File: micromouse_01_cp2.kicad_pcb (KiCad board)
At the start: 4 copper layers, 52 x 51.4 mm, 109 parts, among them IC2 MPU-6500, IC5 DRV8835DSSR, IC6 PCA9632TK,118, J1 Conn_01x02_Pin, J2 Fan+, J4 Fan-, M1 MK06-4.5, M2 MK06-4.5, Q1 MCM3400A-TP, Q2 MCM3400A-TP, Q3 MCM3400A-TP, Q4 Q_PMOS_GSD, Q5 Q_PMOS_GSD, Q6 Q_PMOS_GSD, SW3 SSSS810701, U1 SMT-0440-S-R, U10 MA730, U11 MA730, U13 MCP3464T-E/NC, U2 LBR-127HLD, U3 LBR-127HLD, U4 LBR-127HLD, U5 LBR-127HLD, U6 LXDC55FAAA-203, U7 MCP73831-2-OT, U8 WS2812-2020, U9 ESP32-S3-PICO-1-N8R2

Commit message: 新しい部品乗せた
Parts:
- removed the C21 at (151.9, 58.7)
- removed the C22 at (150.3, 58.4)
- removed the C23 at (149.4, 58.4)
- removed the C24 at (148.4, 59.6)
- removed the C6 at (153.8, 62.1)
- removed the C7 at (154.8, 60.3)
- removed the J1 at (147.3, 85.4)
- removed the Q2 at (160.7, 66.1)
- removed the Q3 at (161.3, 100.3)
- removed the R10 at (161.8, 63.8)
- removed the R11 at (161.4, 67.9)
- removed the R12 at (167.7, 69.6)
- removed the R13 at (160.2, 64.3)
- removed the R14 at (158.6, 66.1)
- removed the R15 at (157.6, 66.1)
- removed the R20 at (153.7, 60.0)
- removed the R4 at (143.4, 67.9)
- removed the R5 at (140.4, 63.4)
- removed the R7 at (141.3, 67.7)
- removed the R8 at (144.4, 66.9)
- removed the R9 at (133.3, 68.4)
- removed U13: MCP3464T-E/NC, footprints:UQFN20_NC_MCH
- removed the U2 at (140.9, 59.7)
- removed the U3 at (136.4, 62.3)
- removed the U4 at (165.6, 62.3)
- removed the U5 at (161.1, 59.7)
- added C18: 1u, Capacitor_SMD:C_0402_1005Metric, F.Cu at (148.0, 60.6)
- added C19: 1u, Capacitor_SMD:C_0402_1005Metric, F.Cu at (148.3, 62.5)
- added C2: ~, Capacitor_SMD:C_0402_1005Metric, F.Cu at (140.0, 100.3)
- added C26: 0.1u, Capacitor_SMD:C_0402_1005Metric, F.Cu at (154.5, 59.3)
- added C27: 22u, Capacitor_SMD:C_0603_1608Metric, F.Cu at (143.1, 67.4)
- added C28: 22u, Capacitor_SMD:C_0603_1608Metric, F.Cu at (133.5, 73.0)
- added C29: 22u, Capacitor_SMD:C_0603_1608Metric, F.Cu at (160.7, 68.3)
- added C3: ~, Capacitor_SMD:C_0402_1005Metric, F.Cu at (141.4, 100.8)
- added C30: 22u, Capacitor_SMD:C_0603_1608Metric, F.Cu at (168.7, 72.8)
- added IC3: ADS7066IRTER, footprints:QFN50P300X300X80-17N-D, F.Cu at (151.0, 60.2)
- added J4: Battery, footprints:MK06-4.5, F.Cu at (147.3, 85.6)
- added Q5: SiA519, Package_TO_SOT_SMD:Vishay_PowerPAK_SC70-6L_Dual, F.Cu at (141.0, 65.4)
- added Q6: SiA519, Package_TO_SOT_SMD:Vishay_PowerPAK_SC70-6L_Dual, F.Cu at (133.8, 70.3)
- added Q7: SiA519, Package_TO_SOT_SMD:Vishay_PowerPAK_SC70-6L_Dual, F.Cu at (161.0, 65.4)
- added Q8: SiA519, Package_TO_SOT_SMD:Vishay_PowerPAK_SC70-6L_Dual, F.Cu at (168.4, 69.8)
- added R21: 22, Resistor_SMD:R_0402_1005Metric, F.Cu at (140.7, 67.1)
- added R23: 22, Resistor_SMD:R_0402_1005Metric, F.Cu at (133.5, 71.8)
- added R24: １ｋ, Resistor_SMD:R_0402_1005Metric, F.Cu at (139.9, 63.3)
- added R25: 22, Resistor_SMD:R_0402_1005Metric, F.Cu at (161.8, 67.7)
- added R26: １ｋ, Resistor_SMD:R_0402_1005Metric, F.Cu at (157.3, 66.4)
- added R27: 22, Resistor_SMD:R_0402_1005Metric, F.Cu at (169.2, 71.7)
- added R28: １ｋ, Resistor_SMD:R_0402_1005Metric, F.Cu at (166.6, 67.3)
- added U10: LBR-127HLD, footprints:LBR-127HLD, F.Cu at (161.1, 59.7)
- added U11: LBR-127HLD, footprints:LBR-127HLD, F.Cu at (165.6, 62.3)
- added U8: LBR-127HLD, footprints:LBR-127HLD, F.Cu at (140.9, 59.7)
- added U9: LBR-127HLD, footprints:LBR-127HLD, F.Cu at (136.4, 62.3)
- C17: value 0.1u -> 1u
- D10: renamed from D6; value PWR -> POWER
- Q1: value MCM3400A-TP -> SiA910; footprint footprints:DFN2020-6L_MCE -> Package_TO_SOT_SMD:Vishay_PowerPAK_SC70-6L_Dual
- R1: renamed from R33; value 22 -> 0
- R2: renamed from R32; value 22 -> 0
- R22: value 47k -> １ｋ
- R5: renamed from R17; value 47k -> 47k
- R6: value 1k -> 47k
- moved R22 46.0 mm to (146.6, 59.4), turned to 90 degrees
- moved R6 45.2 mm to (163.8, 101.8)
- moved Q1 39.8 mm to (161.1, 100.2), turned to 0 degrees
- moved C20 28.6 mm to (162.2, 70.0), turned to 90 degrees
- moved U5 26.7 mm to (160.3, 71.2), turned to 180 degrees
- moved R2 2.23 mm to (141.4, 99.9), turned to 180 degrees
- moved C17 1.80 mm to (149.8, 62.8), turned to 180 degrees
- moved R1 1.60 mm to (140.5, 99.0)
- moved C22 1.10 mm to (142.0, 95.3)
- moved R10 0.95 mm to (144.3, 95.0)
- moved IC4 0.85 mm to (159.8, 96.4)
- moved U6 0.60 mm to (142.7, 92.5)
- moved U4 0.34 mm to (168.9, 105.1)
- moved C6 0.23 mm to (140.2, 69.3)
- moved SW1 0.15 mm to (163.1, 103.8)
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- renumbered C14 to C1, C37 to C10, C38 to C11, C41 to C12, C15 to C13, C16 to C14, C9 to C15, C25 to C16, C8 to C20, C19 to C21, C18 to C22, C2 to C23, C13 to C24, C10 to C25, C12 to C4, C3 to C5, C5 to C6, C4 to C7, C20 to C8, C1 to C9, D1 to D2, D4 to D3, D3 to D4, D8 to D5, D9 to D6, D10 to D7, D5 to D8, D7 to D9, IC2 to IC1, IC5 to IC2, IC6 to IC4, J3 to J1, J4 to J3, Q4 to Q2, Q5 to Q3, Q6 to Q4, R28 to R10, R30 to R11, R31 to R12, R24 to R13, R1 to R14, R27 to R15, R2 to R16, R23 to R17, R16 to R18, R18 to R19, R19 to R20, R21 to R3, R3 to R4, R29 to R7, R25 to R8, R26 to R9, SW3 to SW1, U10 to U1, U11 to U2, U9 to U3, U1 to U4, U8 to U5, U7 to U6, U6 to U7
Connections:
- C17 pad 1: VBATT -> +3V3
- D2 pad 2: Net-(D1-A) -> Net-(D2-A)
- J3 pad 1: Net-(J4-Pin_1) -> Net-(J3-Pin_1)
- Q1 pad 2: LED_L -> BUZZER
- Q1 pad 3: Net-(Q1-Pad3) -> Net-(J3-Pin_1)
- Q1 pad 5: LED_FL -> FAN_PWM
- Q1 pad 6: Net-(Q1-Pad6) -> Net-(D2-A)
- R22 pad 1: FAN_PWM -> SENS_L
- R6 pad 1: SENS_L -> GND
- R6 pad 2: GND -> FAN_PWM
- U3 pad 7: IMU_MISO -> IMU_MOSI
- U3 pad 8: IMU_MOSI -> IMU_CLK
- U3 pad 9: IMU_CLK -> IMU_MISO
- U4 pad 2: Net-(D1-A) -> Net-(D2-A)
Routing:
- net GND: track 96.2 -> 49.8 mm, vias 283 -> 230
- net NeoPixel: track 17.0 -> 0.97 mm, vias 0 -> 1
- net Net-(C27-Pad1): track 0.00 -> 12.2 mm, vias 0 -> 2
- net Net-(D2-A): track 0.00 -> 10.5 mm
- net Net-(D1-A): track 10.3 -> 0.00 mm
- net Net-(Q7-Pad6): track 0.00 -> 9.97 mm, vias 0 -> 1
- net VBATT: track 61.3 -> 51.7 mm, vias 3 -> 2
- net Net-(C29-Pad1): track 0.00 -> 9.12 mm, vias 0 -> 1
- net Net-(R5-Pad1): track 8.69 -> 0.00 mm
- net Net-(R13-Pad1): track 8.23 -> 0.00 mm, vias 1 -> 0
- net SENS_FL: track 26.4 -> 18.4 mm
- net Net-(R7-Pad1): track 8.03 -> 0.00 mm
- net Net-(Q5-Pad6): track 0.00 -> 7.62 mm
- net Net-(C28-Pad1): track 0.00 -> 6.61 mm, vias 0 -> 1
- net Net-(Q8-Pad6): track 0.00 -> 6.57 mm
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- added copper zone on F.Cu, net Net-(D7-K)
- removed copper zone on F.Cu, net Net-(D9-K)
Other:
- outline, holes or cut-outs redrawn

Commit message: PCB設計完了（仮）
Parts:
- moved C20 0.92 mm to (161.9, 69.1)
- moved R12 0.54 mm to (152.9, 106.6)
- moved R18 0.53 mm to (156.9, 107.1)
- moved D10 0.50 mm to (155.1, 107.1)
- moved D6 0.47 mm to (152.0, 105.5)
- moved C29 0.45 mm to (160.7, 67.9)
- moved R11 0.45 mm to (151.1, 106.6)
- moved Q7 0.40 mm to (161.0, 65.0)
- moved R9 0.39 mm to (150.2, 106.6)
- moved R25 0.35 mm to (161.9, 67.3)
- moved C19 0.35 mm to (148.4, 62.2)
- moved C18 0.32 mm to (148.1, 60.3)
- moved D7 0.30 mm to (155.0, 105.5)
- moved R8 0.28 mm to (148.4, 106.6)
- moved D5 0.28 mm to (149.3, 105.5)
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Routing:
- net +3V3: track 252.4 -> 274.0 mm, vias 38 -> 47
- net NeoPixel: track 0.97 -> 19.4 mm, vias 1 -> 2
- net FAN_PWM: track 46.3 -> 59.6 mm
- net GND: track 49.8 -> 47.4 mm, vias 230 -> 310
- net IMU_MISO: track 28.1 -> 29.1 mm
- net LED_FR: track 26.3 -> 27.2 mm
- net LED_R: track 24.3 -> 25.2 mm
- net Net-(C27-Pad1): track 12.2 -> 11.6 mm
- net ENCL_CS: track 25.5 -> 24.9 mm
- added copper zone on F.Cu, net Net-(D9-K)
- added copper zone on F.Cu, net Net-(J3-Pin_1)
- removed copper zone on F.Cu, net Net-(D7-K)

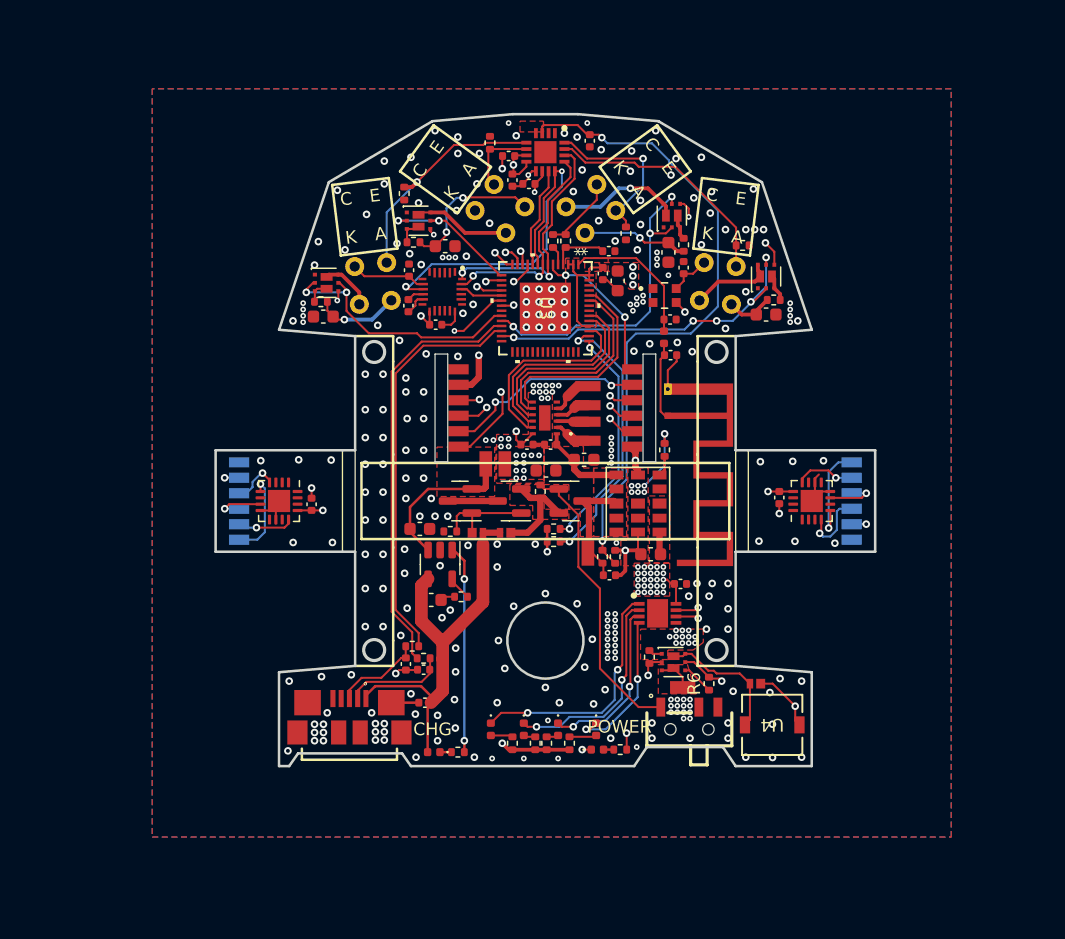
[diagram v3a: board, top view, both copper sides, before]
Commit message: [fix]ブザー向きを修正
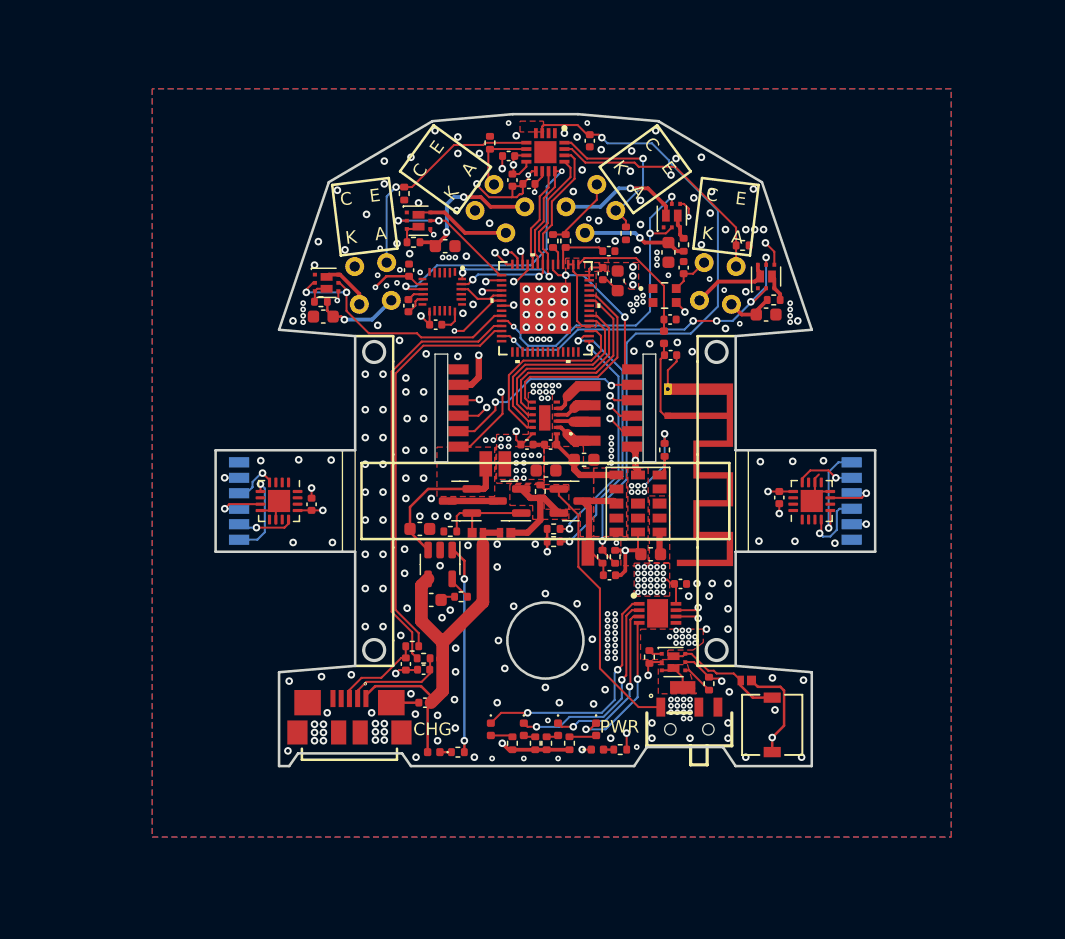
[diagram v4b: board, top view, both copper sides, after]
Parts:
- D10: value POWER -> PWR
- moved D2 0.77 mm to (166.9, 101.7)
- turned U4 to 90 degrees
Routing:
- net GND: track 47.4 -> 53.0 mm, vias 310 -> 322
- net BUZZER: track 41.3 -> 40.2 mm
- net Net-(D2-A): track 10.5 -> 9.53 mm
- net LED_R: track 25.2 -> 26.1 mm
- net LED_FR: track 27.2 -> 28.0 mm
- net +3V3: track 274.0 -> 274.7 mm, vias 47 -> 48
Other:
- board text added: "reRoMouse v1.1 2024 Apr Designed by Yujiro & Saposen"
- board text removed: "reRoMouse v1.0 2024 Mar made by Yujiro & Saposen"

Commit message: Lipo接続パッド修正
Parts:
- moved J4 1.15 mm to (148.4, 85.7)
- moved C9 0.79 mm to (148.9, 82.6), turned to -90 degrees
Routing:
- net GND: track 53.0 -> 52.1 mm, vias 322 -> 324
- net +3V3: track 274.7 -> 275.2 mm

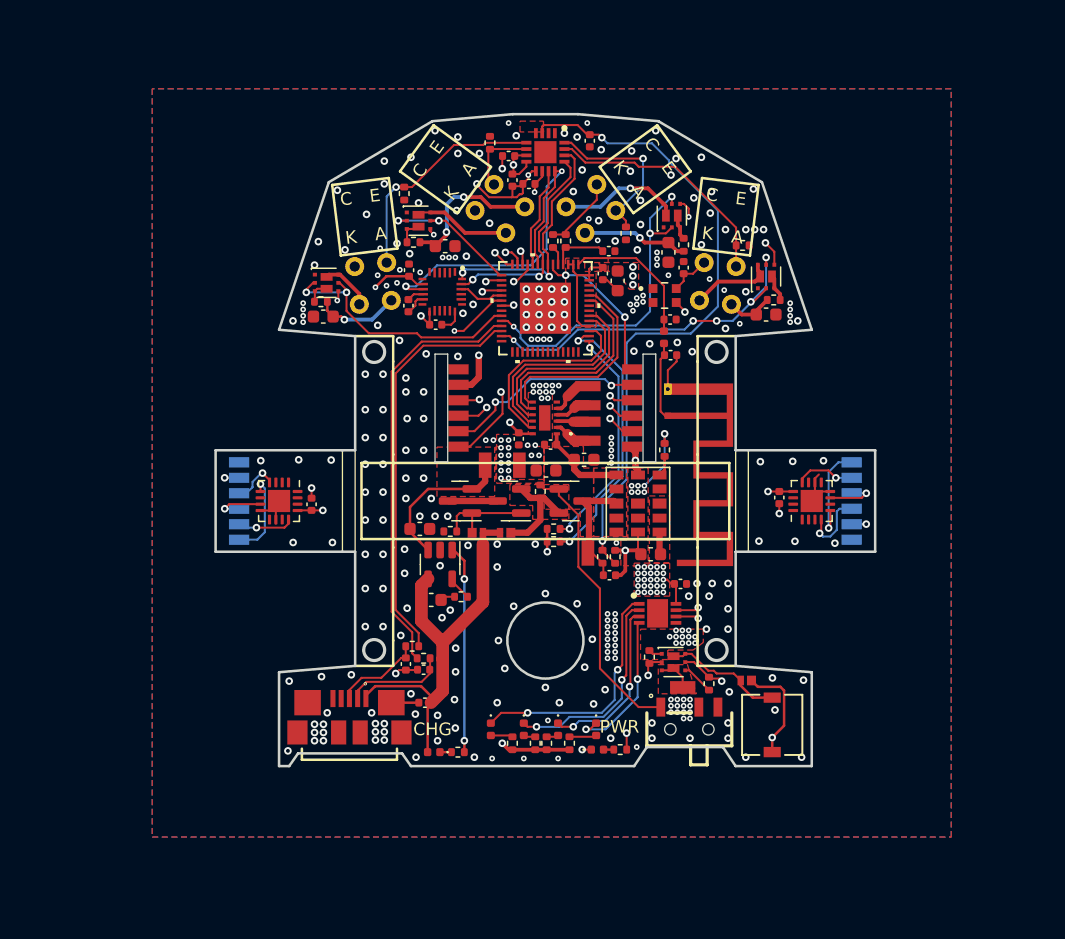
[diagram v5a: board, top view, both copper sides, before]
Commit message: 回路図完成 PCB配線途中
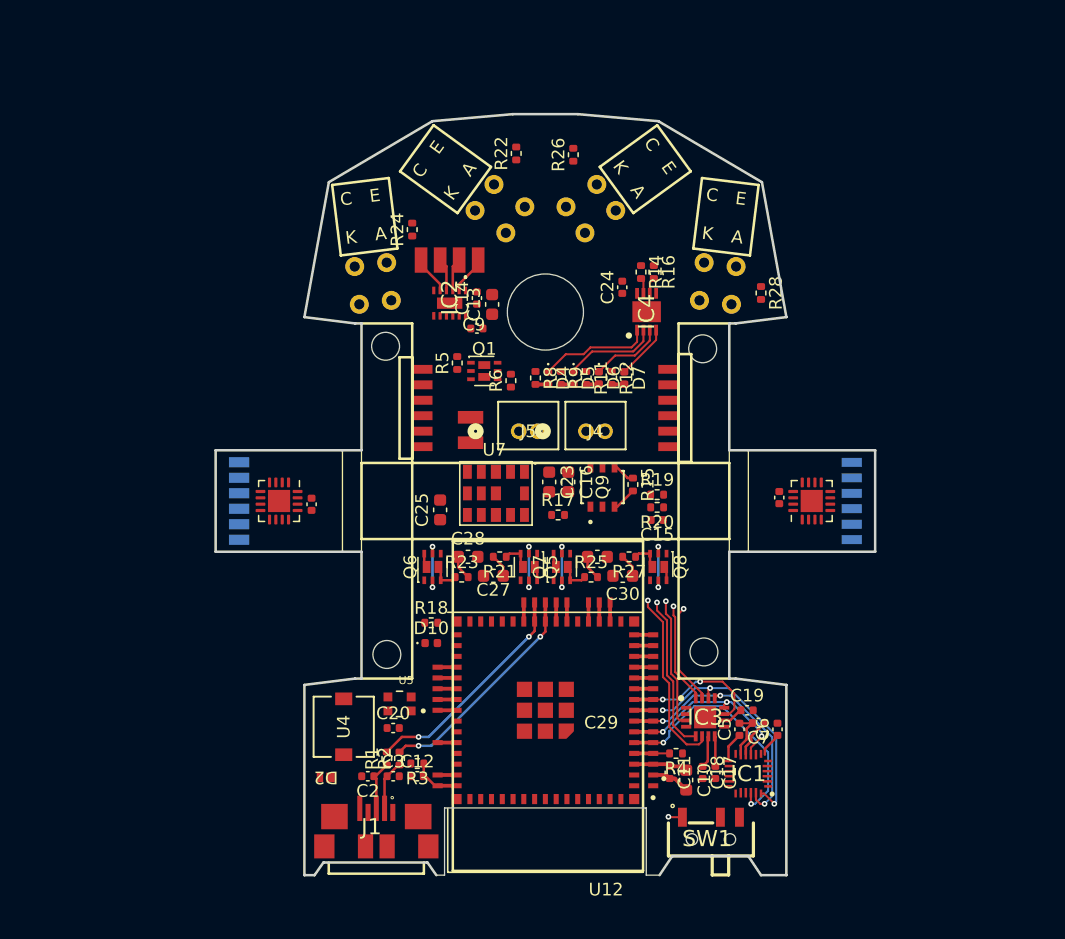
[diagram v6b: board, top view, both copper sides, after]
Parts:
- removed AE1: Antenna_Shield, RF_Antenna:Texas_SWRA117D_2.4GHz_Right
- removed C1, C26: 0.1u, Capacitor_SMD:C_0402_1005Metric
- removed the C11 at (155.5, 69.6)
- removed the C11 at (156.1, 93.3)
- removed C21, C22: 4.7u, Capacitor_SMD:C_0603_1608Metric
- removed D3: LED, LED_SMD:LED_0402_1005Metric
- removed D8, D9: CCS15S40,L3F, footprints:SOD-963 CST2C_TOS
- removed L1: 2.2n, Inductor_SMD:L_0402_1005Metric
- removed Q2, Q3, Q4: Q_PMOS_GSD, Package_TO_SOT_SMD:SOT-23
- removed R10: 47k, Resistor_SMD:R_0402_1005Metric
- removed R13: 1k, Resistor_SMD:R_0402_1005Metric
- removed R7: 470, Resistor_SMD:R_0402_1005Metric
- removed U3: ESP32-S3-PICO-1-N8R2, footprints:QFN56_7X7_EXP
- removed U6: MCP73831-2-OT, Package_TO_SOT_SMD:SOT-23-5
- added C11: 0.1u, Capacitor_SMD:C_0402_1005Metric, F.Cu at (160.8, 108.9)
- added J5: Battery, footprints:CONN_B2B-ZRLFSN_JST, F.Cu at (148.9, 82.0)
- added Q9: SSM6J808R_LXHF, footprints:TSOP6F_SSM6J_TOS, F.Cu at (155.5, 86.4)
- added U12: ESP32-S3-MINI-1-N8, footprints:XCVR_ESP32-S3-MINI-1-N8, F.Cu at (151.0, 104.0)
- C15: value 3.3p -> 0.1u
- C16: value 3.3p -> 22u; footprint Capacitor_SMD:C_0402_1005Metric -> Capacitor_SMD:C_0603_1608Metric
- D10: value PWR -> POWER
- J4: footprint footprints:MK06-4.5 -> footprints:CONN_B2B-ZRLFSN_JST
- R15: value 1k -> 47k
- moved C18 51.0 mm to (163.4, 108.9), turned to -90 degrees
- moved C17 48.7 mm to (164.4, 108.9), turned to -90 degrees
- moved C6 46.4 mm to (169.3, 105.5)
- moved IC3 46.3 mm to (163.6, 104.5), turned to 0 degrees
- moved C19 45.7 mm to (166.9, 104.0), turned to 0 degrees
- moved IC1 45.0 mm to (167.0, 109.0), turned to 180 degrees
- moved C12 44.1 mm to (140.9, 109.2), turned to 0 degrees
- moved C7 42.9 mm to (167.8, 105.0), turned to 180 degrees
- moved C20 42.9 mm to (139.0, 105.4), turned to 0 degrees
- moved R3 42.8 mm to (140.9, 108.2), turned to 180 degrees
- moved R4 41.5 mm to (161.3, 107.4), turned to 180 degrees
- moved C5 39.9 mm to (166.3, 105.5), turned to 90 degrees
- moved C10 39.7 mm to (162.1, 109.5)
- moved U5 38.4 mm to (139.5, 103.5), turned to 0 degrees
- moved D2 34.0 mm to (133.7, 109.3)
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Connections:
- net /CHIP_PU renamed /EN
- C15 pad 1: Net-(AE1-A) -> VBATT
- C16 pad 1: Net-(U3-LNA_IN) -> +BATT
- J1 pad 1: VBUS -> unconnected-(J1-VBUS-Pad1)
- J4 pad 1: GND -> Net-(J4-Pin_1)
- R15 pad 1: Net-(D9-K) -> Net-(J4-Pin_2)
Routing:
- net +3V3: track 275.2 -> 15.2 mm, vias 48 -> 0
- net FAN_PWM: track 59.6 -> 1.50 mm, vias 2 -> 0
- net GND: track 52.1 -> 7.00 mm, vias 324 -> 0
- net VBATT: track 51.8 -> 10.4 mm, vias 2 -> 1
- net BUZZER: track 40.2 -> 1.50 mm, vias 2 -> 0
- net ENC_CLK: track 38.8 -> 1.50 mm, vias 5 -> 0
- net ENC_MOSI: track 38.2 -> 1.50 mm, vias 5 -> 0
- net ENC_MISO: track 37.2 -> 1.50 mm, vias 5 -> 0
- net LED_SCL: track 36.1 -> 2.80 mm, vias 3 -> 0
- net VBUS: track 32.9 -> 0.00 mm
- net LED_SDA: track 33.2 -> 2.75 mm, vias 3 -> 0
- net ENCL_CS: track 24.9 -> 1.50 mm, vias 3 -> 0
- net LED_FR: track 28.0 -> 5.80 mm, vias 5 -> 2
- net LED_R: track 26.1 -> 5.80 mm, vias 3 -> 2
- net Net-(Q9-G): track 23.1 -> 3.08 mm, vias 0 -> 1
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- removed copper zone on F.Cu, net +3V3
- removed copper zone on In1.Cu, net +3V3
- removed copper zone on F.Cu, net +BATT
- removed copper zone on B.Cu, net GND
- removed copper zone on F.Cu, net GND
- removed copper zone on In1.Cu, net GND
- removed copper zone on In2.Cu, net GND
- removed copper zone on F.Cu, net Net-(D9-K)
- removed copper zone on F.Cu, net Net-(J3-Pin_1)
- removed copper zone on F.Cu, net Net-(J4-Pin_2)
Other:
- board size 52 x 51.4 mm -> 52 x 60 mm
